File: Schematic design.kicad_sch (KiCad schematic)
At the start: 74 parts, among them J1 USB4105-GF-A-120, J2 MOLEX 53261-0571, J4 MOLEX 51021-0200, U1 MAX30101, U10 MCP73832-2-OT, U11 TPD4S014DSQR, U2 PCA9306DCUR, U3 LIS3MDL, U4 TLV61070ADBV, U5 TPS7A0518PDBV, U6 TPS7A0533PDBV, U7 MDBT50Q-1MV2, U9 MPU-6500, Y1 FC-135R 32.7680KA-AC3

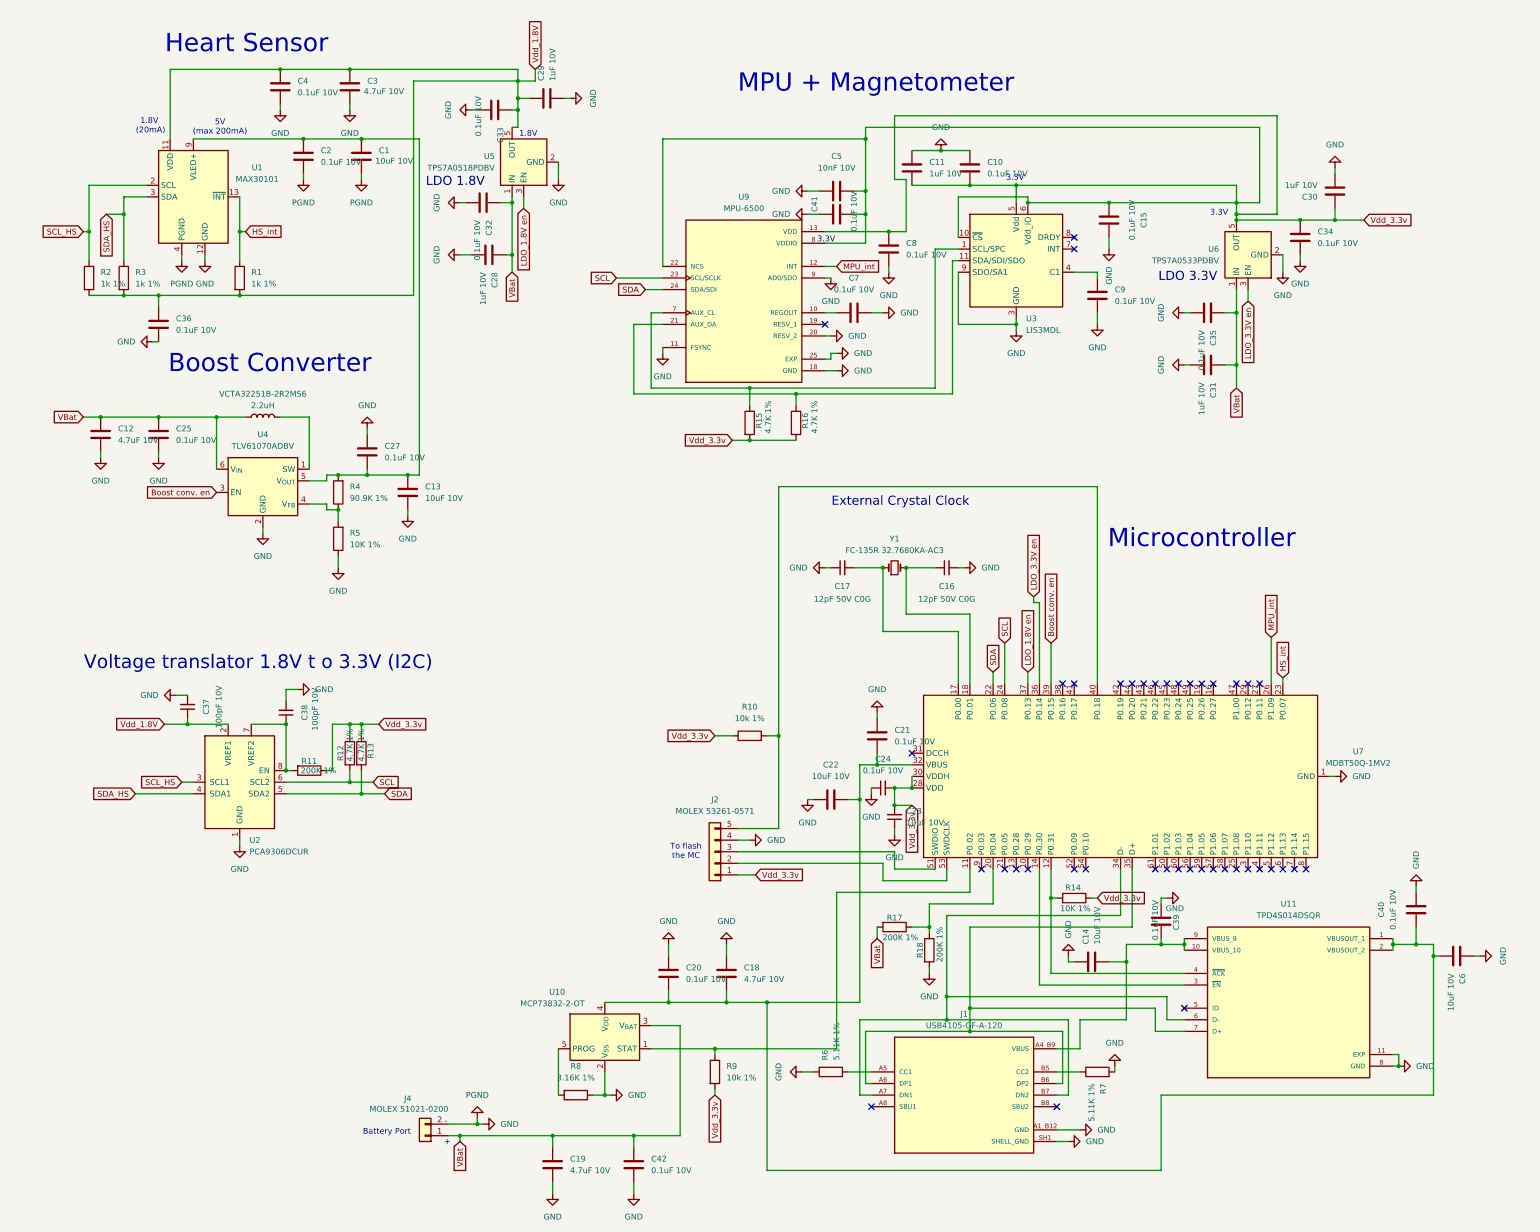
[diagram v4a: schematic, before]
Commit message: First Final PCB and Schematic of the wearable
Changed some circuitry around a little bit to complete the PCB traces and triple checked the PCB against the schematic while considering PCB design norms and rules. Overall the wearable device PCB seems to be done. The gerber, drill, BOM and pick-and-place files have been sent to be manufactured so I can better understand and deal with physical realities.  PCBWay is currently being used.
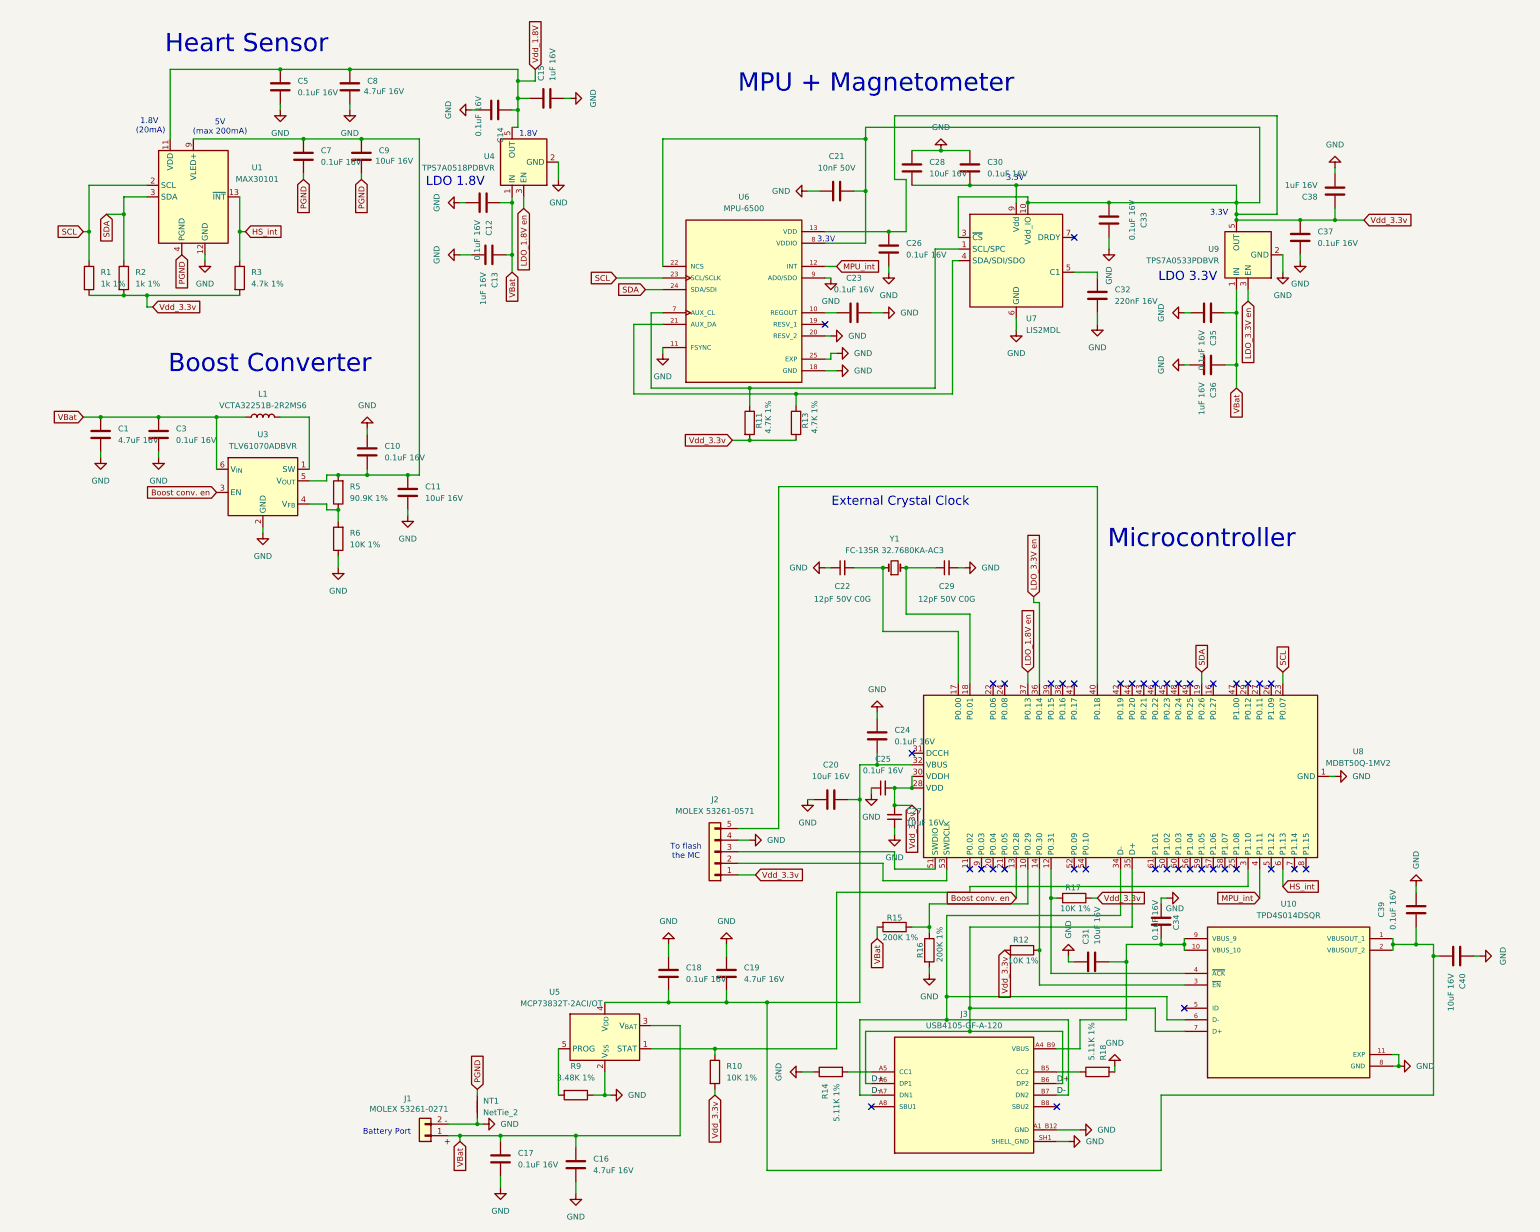
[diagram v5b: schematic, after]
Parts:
- removed C36, C41: 0.1uF 10V, Capacitor_SMD:C_0402_1005Metric, symbol Device:C
- removed C37, C38: 100pF 10V, Capacitor_SMD:C_0402_1005Metric, symbol Device:C_Small
- removed R10: 10k 1%, Resistor_SMD:R_0402_1005Metric, symbol Device:R
- removed R11: 200K 1%, Resistor_SMD:R_0402_1005Metric, symbol Device:R
- removed R13: 4.7K 1%, Resistor_SMD:R_0402_1005Metric, symbol Device:R
- removed U2: PCA9306DCUR, Package_SO:VSSOP-8_2.3x2mm_P0.5mm, symbol Interface:PCA9306DC1
- removed U3: LIS3MDL, Package_LGA:LGA-12_2x2mm_P0.5mm, symbol Sensor_Magnetic:LIS3MDL
- added NT1: NetTie_2, symbol Device:NetTie_2
- added U7: LIS2MDL, Package_LGA:LGA-12_2x2mm_P0.5mm, symbol Sensor_Magnetic:LIS2MDL
- C1: renamed from C12; value 4.7uF 10V -> 4.7uF 16V; MPN (none) -> CL10A475KO8NQNC; Manufacturer (none) -> Samsung Electro-Mechanics; Type (none) -> SMD
- C10: renamed from C27; value 0.1uF 10V -> 0.1uF 16V; MPN (none) -> CL05A104KO5NNNC; Manufacturer (none) -> Samsung Electro-Mechanics; Type (none) -> SMD
- C11: renamed from C13; value 10uF 10V -> 10uF 16V; MPN (none) -> CL10A106MO8NRNC; Manufacturer (none) -> Samsung Electro-Mechanics; Type (none) -> SMD
- C12: renamed from C32; value 0.1uF 10V -> 0.1uF 16V; MPN (none) -> CL05A104KO5NNNC; Manufacturer (none) -> Samsung Electro-Mechanics; Type (none) -> SMD
- C13: renamed from C28; value 1uF 10V -> 1uF 16V; MPN (none) -> CL10A105KO8NNNC; Manufacturer (none) -> Samsung Electro-Mechanics; Type (none) -> SMD
- C14: renamed from C33; value 0.1uF 10V -> 0.1uF 16V; MPN (none) -> CL05A104KO5NNNC; Manufacturer (none) -> Samsung Electro-Mechanics; Type (none) -> SMD
- C15: renamed from C29; value 1uF 10V -> 1uF 16V; MPN (none) -> CL10A105KO8NNNC; Manufacturer (none) -> Samsung Electro-Mechanics; Type (none) -> SMD
- C16: renamed from C19; value 4.7uF 10V -> 4.7uF 16V; MPN (none) -> CL10A475KO8NQNC; Manufacturer (none) -> Samsung Electro-Mechanics; Type (none) -> SMD
- C17: renamed from C42; value 0.1uF 10V -> 0.1uF 16V; MPN (none) -> CL05A104KO5NNNC; Manufacturer (none) -> Samsung Electro-Mechanics; Type (none) -> SMD
- C18: renamed from C20; value 0.1uF 10V -> 0.1uF 16V; MPN (none) -> CL05A104KO5NNNC; Manufacturer (none) -> Samsung Electro-Mechanics; Type (none) -> SMD
- C19: renamed from C18; value 4.7uF 10V -> 4.7uF 16V; MPN (none) -> CL10A475KO8NQNC; Manufacturer (none) -> Samsung Electro-Mechanics; Type (none) -> SMD
- C20: renamed from C22; value 10uF 10V -> 10uF 16V; MPN (none) -> CL10A106MO8NRNC; Manufacturer (none) -> Samsung Electro-Mechanics; Type (none) -> SMD
- C21: renamed from C5; value 10nF 10V -> 10nF 50V; MPN (none) -> CL05B103KB5NNNC; Manufacturer (none) -> Samsung Electro-Mechanics; Type (none) -> SMD
- C22: renamed from C17; MPN (none) -> CL05C120JB5NNNC; Manufacturer (none) -> Samsung Electro-Mechanics; Type (none) -> SMD
- C23: renamed from C7; value 0.1uF 10V -> 0.1uF 16V; MPN (none) -> CL05A104KO5NNNC; Manufacturer (none) -> Samsung Electro-Mechanics; Type (none) -> SMD
- C24: renamed from C21; value 0.1uF 10V -> 0.1uF 16V; MPN (none) -> CL05A104KO5NNNC; Manufacturer (none) -> Samsung Electro-Mechanics; Type (none) -> SMD
- C25: renamed from C24; value 0.1uF 10V -> 0.1uF 16V; MPN (none) -> CL05A104KO5NNNC; Manufacturer (none) -> Samsung Electro-Mechanics; Type (none) -> SMD
- C26: renamed from C8; value 0.1uF 10V -> 0.1uF 16V; MPN (none) -> CL05A104KO5NNNC; Manufacturer (none) -> Samsung Electro-Mechanics; Type (none) -> SMD
- C27: renamed from C23; value 10uF 10V -> 10uF 16V; MPN (none) -> CL10A106MO8NRNC; Manufacturer (none) -> Samsung Electro-Mechanics; Type (none) -> SMD
- C28: renamed from C11; value 1uF 10V -> 10uF 16V; footprint Capacitor_SMD:C_0402_1005Metric -> Capacitor_SMD:C_0603_1608Metric; MPN (none) -> CL10A106MO8NRNC; Manufacturer (none) -> Samsung Electro-Mechanics; Type (none) -> SMD
- C29: renamed from C16; MPN (none) -> CL05C120JB5NNNC; Manufacturer (none) -> Samsung Electro-Mechanics; Type (none) -> SMD
- C3: renamed from C25; value 0.1uF 10V -> 0.1uF 16V; MPN (none) -> CL05A104KO5NNNC; Manufacturer (none) -> Samsung Electro-Mechanics; Type (none) -> SMD
- C30: renamed from C10; value 0.1uF 10V -> 0.1uF 16V; MPN (none) -> CL05A104KO5NNNC; Manufacturer (none) -> Samsung Electro-Mechanics; Type (none) -> SMD
- C31: renamed from C14; value 10uF 10V -> 10uF 16V; MPN (none) -> CL10A106MO8NRNC; Manufacturer (none) -> Samsung Electro-Mechanics; Type (none) -> SMD
- C32: renamed from C9; value 0.1uF 10V -> 220nF 16V; MPN (none) -> CL05B224KO5NNNC; Manufacturer (none) -> Samsung Electro-Mechanics; Type (none) -> SMD
- C33: renamed from C15; value 0.1uF 10V -> 0.1uF 16V; MPN (none) -> CL05A104KO5NNNC; Manufacturer (none) -> Samsung Electro-Mechanics; Type (none) -> SMD
- C34: renamed from C39; value 0.1uF 10V -> 0.1uF 16V; MPN (none) -> CL05A104KO5NNNC; Manufacturer (none) -> Samsung Electro-Mechanics; Type (none) -> SMD
- C35: value 0.1uF 10V -> 0.1uF 16V; MPN (none) -> CL05A104KO5NNNC; Manufacturer (none) -> Samsung Electro-Mechanics; Type (none) -> SMD
- C36: renamed from C31; value 1uF 10V -> 1uF 16V; MPN (none) -> CL10A105KO8NNNC; Manufacturer (none) -> Samsung Electro-Mechanics; Type (none) -> SMD
- C37: renamed from C34; value 0.1uF 10V -> 0.1uF 16V; MPN (none) -> CL05A104KO5NNNC; Manufacturer (none) -> Samsung Electro-Mechanics; Type (none) -> SMD
- C38: renamed from C30; value 1uF 10V -> 1uF 16V; MPN (none) -> CL10A105KO8NNNC; Manufacturer (none) -> Samsung Electro-Mechanics; Type (none) -> SMD
- C39: renamed from C40; value 0.1uF 10V -> 0.1uF 16V; MPN (none) -> CL05A104KO5NNNC; Manufacturer (none) -> Samsung Electro-Mechanics; Type (none) -> SMD
- C40: renamed from C6; value 10uF 10V -> 10uF 16V; MPN (none) -> CL10A106MO8NRNC; Manufacturer (none) -> Samsung Electro-Mechanics; Type (none) -> SMD
- C5: renamed from C4; value 0.1uF 10V -> 0.1uF 16V; MPN (none) -> CL05A104KO5NNNC; Manufacturer (none) -> Samsung Electro-Mechanics; Type (none) -> SMD
- C7: renamed from C2; value 0.1uF 10V -> 0.1uF 16V; MPN (none) -> CL05A104KO5NNNC; Manufacturer (none) -> Samsung Electro-Mechanics; Type (none) -> SMD
- C8: renamed from C3; value 4.7uF 10V -> 4.7uF 16V; MPN (none) -> CL10A475KO8NQNC; Manufacturer (none) -> Samsung Electro-Mechanics; Type (none) -> SMD
- C9: renamed from C1; value 10uF 10V -> 10uF 16V; MPN (none) -> CL10A106MO8NRNC; Manufacturer (none) -> Samsung Electro-Mechanics; Type (none) -> SMD
- J1: renamed from J4; value MOLEX 51021-0200 -> MOLEX 53261-0271; MPN (none) -> 53261-0271; Manufacturer (none) -> Molex; Type (none) -> SMD
- J2: MPN (none) -> 53261-0571; Manufacturer (none) -> Molex; Type (none) -> SMD
- J3: renamed from J1; MPN (none) -> USB4105-GF-A-120; Manufacturer (none) -> GCT (Global Connector Technology); Type (none) -> Hybrid
- L1: renamed from VCTA32251B-2R2MS6; value 2.2uH -> VCTA32251B-2R2MS6; MPN (none) -> VCTA32251B-2R2MS6; Manufacturer (none) -> Delta Electronics / Cyntec; Type (none) -> SMD
- R1: renamed from R2; MPN (none) -> RC0402FR-071KL; Manufacturer (none) -> YAGEO; Type (none) -> SMD
- R10: renamed from R9; value 10k 1% -> 10K 1%; MPN (none) -> RC0402FR-0710KL; Manufacturer (none) -> YAGEO; Type (none) -> SMD
- R11: renamed from R15; MPN (none) -> RC0402FR-074K7L; Manufacturer (none) -> YAGEO; Type (none) -> SMD
- R12: value 4.7K 1% -> 10K 1%; MPN (none) -> RC0402FR-0710KL; Manufacturer (none) -> YAGEO; Type (none) -> SMD
- R13: renamed from R16; MPN (none) -> RC0402FR-074K7L; Manufacturer (none) -> YAGEO; Type (none) -> SMD
- R14: renamed from R6; MPN (none) -> RC0402FR-075K11L; Manufacturer (none) -> YAGEO; Type (none) -> SMD
- R15: renamed from R17; MPN (none) -> RC0402FR-07200KL; Manufacturer (none) -> YAGEO; Type (none) -> SMD
- R16: renamed from R18; MPN (none) -> RC0402FR-07200KL; Manufacturer (none) -> YAGEO; Type (none) -> SMD
- R17: renamed from R14; MPN (none) -> RC0402FR-0710KL; Manufacturer (none) -> YAGEO; Type (none) -> SMD
- R18: renamed from R7; MPN (none) -> RC0402FR-075K11L; Manufacturer (none) -> YAGEO; Type (none) -> SMD
- R2: renamed from R3; MPN (none) -> RC0402FR-071KL; Manufacturer (none) -> YAGEO; Type (none) -> SMD
- R3: renamed from R1; value 1k 1% -> 4.7k 1%; MPN (none) -> RC0402FR-074K7L; Manufacturer (none) -> YAGEO; Type (none) -> SMD
- R5: renamed from R4; MPN (none) -> RC0402FR-0790K9L; Manufacturer (none) -> YAGEO; Type (none) -> SMD
- R6: renamed from R5; MPN (none) -> RC0402FR-0710KL; Manufacturer (none) -> YAGEO; Type (none) -> SMD
- R9: renamed from R8; value 3.16K 1% -> 3.48K 1%; MPN (none) -> RC0402FR-073K48L; Manufacturer (none) -> YAGEO; Type (none) -> SMD
- U1: MPN (none) -> MAX30101EFD+T; Manufacturer (none) -> Analog Devices (Maxim Integrated); Type (none) -> SMD
- U10: renamed from U11; footprint TPD4S014DSQR Footprint:SON40P200X200X80-11N -> TPD4S014DSQR:SON40P200X200X80-11N; MPN (none) -> TPD4S014DSQR; Manufacturer (none) -> Texas Instruments; Type (none) -> SMD
- U3: renamed from U4; value TLV61070ADBV -> TLV61070ADBVR; MPN (none) -> TLV61070ADBVR; Manufacturer (none) -> Texas Instruments; Type (none) -> SMD
- U4: renamed from U5; value TPS7A0518PDBV -> TPS7A0518PDBVR; MPN (none) -> TPS7A0518PDBVR; Manufacturer (none) -> Texas Instruments; Type (none) -> SMD
- U5: renamed from U10; value MCP73832-2-OT -> MCP73832T-2ACI/OT; MPN (none) -> MCP73832T-2ACI/OT; Manufacturer (none) -> Microchip Technology; Type (none) -> SMD
- U6: renamed from U9; MPN (none) -> MPU-6500; Manufacturer (none) -> TDK InvenSense; Type (none) -> SMD
- U8: renamed from U7; MPN (none) -> MDBT50Q-1MV2; Manufacturer (none) -> Raytac Corporation; Type (none) -> SMD
- U9: renamed from U6; value TPS7A0533PDBV -> TPS7A0533PDBVR; MPN (none) -> TPS7A0533PDBVR; Manufacturer (none) -> Texas Instruments; Type (none) -> SMD
- Y1: MPN (none) -> FC-135R 32.7680KA-AC3; Manufacturer (none) -> EPSON (Seiko Epson Corporation); Type (none) -> SMD
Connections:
- net SCL_HS is gone; now on net SCL: R1.1, U1.2 (SCL)
- net SDA_HS is gone; now on net SDA: R2.1, U1.3 (SDA)
- net Boost conv. en: now also U8.13 (P0.28); no longer U8.39 (P0.15)
- net GND: now also NT1.1, U7.6 (GND), U7.8 (GND); no longer C7.2, C9.2, U1.4 (PGND)
- net HS_int: now also U8.6 (P1.13); no longer U8.23 (P0.07)
- net MPU_int: now also U8.4 (P1.11); no longer U8.26 (P1.09)
- net SCL: now also U8.23 (P0.07); no longer R12.2, U8.24 (P0.08)
- net SDA: now also U8.19 (P0.26); no longer U8.22 (P0.06)
- net Vdd_1.8V: no longer R1.2, R2.2, R3.2
- net Vdd_3.3v: now also R1.2, R12.2, R2.2, R3.2, U7.10 (Vdd_IO), U7.3 (~{CS}), U7.9 (Vdd); no longer R12.1
- net at R13.1, U6.21 (AUX_DA): now also U7.4 (SDA/SDI/SDO)
- net at R15.1, R16.1: now also U8.10 (P0.29); no longer U8.20 (P0.04)
- net at C32.2: now also U7.5 (C1)
- net at R10.1, U5.1 (STAT): now also U8.3 (P1.10); no longer U8.11 (P0.02)
- net at U10.3 (~{EN}), U8.14 (P0.30): now also R12.1
- net D-: now reaches J3.A7 (DN1), J3.B7 (DN2), U10.6 (D-), U8.34 (D-)
- net D+: now reaches J3.A6 (DP1), J3.B6 (DP2), U10.7 (D+), U8.35 (D+)
- net at R11.1, U6.7 (AUX_CL): now also U7.1 (SCL/SPC)
- new net PGND: C7.2, C9.2, NT1.2, U1.4 (PGND)
- no-connect marks 41 -> 40
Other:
- note removed: "Voltage translator 1.8V t o 3.3V (I2C)"
- moved on the sheet: C16, C17
